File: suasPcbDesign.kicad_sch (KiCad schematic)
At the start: 96 parts, among them J1 SENSE_IB, J2 USB_C_Receptacle_USB2.0_16P, J3 5V Test Pad, J4 3V3 Test Pad, J5 PWM CTRL, J6 JTAG Pinout, J7 SPI OUT, J8 Conn_02x08_Counter_Clockwise, SW1 SW_SPST, SW2 SW_SPST, SW3 SW_SPST, SW4 SW_SPST, SW5 SW_SPST, SW6 SW_SPST, SW7 SW_SPST, U1 LMR51625DDC, U2 MCP3562RT-E/ST, U3 ESP32-S3-WROOM-1, U4 TLV77733PDBVR, U5 USBLC6-2SC6, U7 LM66100DCK, U8 74HC138, U9 LMV331, X7R_Cap1 1uF, X7R_Cap2 1uF, X7R_Cap3 1uF, X7R_Cap4 0.1uF

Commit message: PCB schematic ready to layout
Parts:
- removed J8: Conn_02x08_Counter_Clockwise, Connector_PinHeader_2.54mm:PinHeader_2x08_P2.54mm_Vertical, symbol Connector_Generic:Conn_02x08_Counter_Clockwise
- added J8: Vbat Test Pad, Connector_Wire:SolderWirePad_1x01_SMD_5x10mm, symbol Connector:Conn_01x01_Pin
- added J9: SPI Interface, Connector_PinHeader_2.54mm:PinHeader_2x08_P2.54mm_Vertical, symbol Connector_Generic:Conn_02x08_Odd_Even
- added JP6: VIN Vbat JPR, Jumper:SolderJumper-2_P1.3mm_Open_Pad1.0x1.5mm, symbol Jumper:SolderJumper_2_Open
- Cout_Cap7: value 1uF -> 10uF
- J3, J4: footprint Connector_Wire:SolderWirePad_1x01_SMD_3x6mm -> Connector_Wire:SolderWirePad_1x01_SMD_5x10mm
- U1: footprint DDC0006A-MFG -> Package_TO_SOT_SMD:TSOT-23-6_HandSoldering
- U2: footprint TSSOP20_ST_MCH -> Package_SO:TSSOP-20_4.4x6.5mm_P0.65mm
- U4: footprint TLV -> Package_TO_SOT_SMD:SOT-23-5_HandSoldering
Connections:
- net GND: now also J9.15 (Pin_15)
- net SPI_CC0: now also J9.5 (Pin_5)
- net SPI_CC1: now also J9.7 (Pin_7)
- net SPI_CC2: now also J9.9 (Pin_9)
- net SPI_E0_N: now also J9.11 (Pin_11)
- net SPI_E1_N: now also J9.13 (Pin_13)
- net SPI_E2: now also J9.3 (Pin_3)
- net SPI_PR0: now also J9.2 (Pin_2)
- net SPI_PR1: now also J9.4 (Pin_4)
- net SPI_PR2: now also J9.6 (Pin_6)
- net SPI_PR3: now also J9.8 (Pin_8)
- net SPI_PR4: now also J9.10 (Pin_10)
- net SPI_PR5: now also J9.12 (Pin_12)
- net SPI_PR6: now also J9.14 (Pin_14)
- net SPI_PR7: now also J9.16 (Pin_16)
- net VDD: now also J9.1 (Pin_1)
- net at Cap_13.1, D9.2, U6.3 (+): now also JP6.2 (B); no longer RV1.2
- net at D9.1, JP4.1 (A), U6.1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: now also J8.1 (Pin_1)
- new net: JP6.1 (A), RV1.2
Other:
- moved on the sheet: Cap_13, D9, JP4, U6

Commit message: Fix fotprints
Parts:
- C1: footprint (none) -> Capacitor_SMD:C_0603_1608Metric_Pad1.08x0.95mm_HandSolder
- JP3, JP5: footprint (none) -> TestPoint:TestPoint_2Pads_Pitch2.54mm_Drill0.8mm
- L1: footprint suasPCBFootprints:L_Wurth_WE-MXGI-5030 -> Inductor_SMD:L_APV_APH1050
- R28: footprint (none) -> Resistor_SMD:R_0603_1608Metric_Pad0.98x0.95mm_HandSolder
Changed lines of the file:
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@@
 			)
 		)
-		(property "Footprint" "suasPCBFootprints:L_Wurth_WE-MXGI-5030"
+		(property "Footprint" "Inductor_SMD:L_APV_APH1050"
 			(at 111.76 44.45 0)
 			(hide yes)
@@
 			)
 		)
-		(property "Datasheet" ""
+		(property "Datasheet" "https://www.codaca.com/Private/pdf/CSAB1050A.pdf"
 			(at 111.76 44.45 0)
 			(hide yes)
@@
 			)
 		)
-		(property "Description" "Inductor"
+		(property "Description" "Inductor (CSAB1050A-150M)"
 			(at 111.76 44.45 0)
 			(hide yes)
@@
 			)
 		)
-		(property "Footprint" ""
+		(property "Footprint" "Resistor_SMD:R_0603_1608Metric_Pad0.98x0.95mm_HandSolder"
 			(at 261.112 73.66 90)
 			(hide yes)
@@
 			)
 		)
-		(property "Footprint" ""
+		(property "Footprint" "Capacitor_SMD:C_0603_1608Metric_Pad1.08x0.95mm_HandSolder"
 			(at 388.3152 46.99 0)
 			(hide yes)
@@
 			)
 		)
-		(property "Footprint" ""
+		(property "Footprint" "TestPoint:TestPoint_2Pads_Pitch2.54mm_Drill0.8mm"
 			(at 205.74 160.02 0)
 			(hide yes)
@@
 			)
 		)
-		(property "Footprint" ""
+		(property "Footprint" "TestPoint:TestPoint_2Pads_Pitch2.54mm_Drill0.8mm"
 			(at 219.71 29.21 0)
 			(hide yes)

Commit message: Do the layout
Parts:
- removed D3: ESD9B3.3ST5G, Diode_SMD:D_SOD-923, symbol Diode:ESD9B3.3ST5G
- removed D4: ESD9B5.0ST5G, Diode_SMD:D_SOD-923, symbol Diode:ESD9B5.0ST5G
- removed D7: LED, LED_SMD:LED_0603_1608Metric_Pad1.05x0.95mm_HandSolder, symbol Device:LED
- removed J3: 5V Test Pad, Connector_Wire:SolderWirePad_1x01_SMD_5x10mm, symbol Connector:Conn_01x01_Pin
- removed J4: 3V3 Test Pad, Connector_Wire:SolderWirePad_1x01_SMD_5x10mm, symbol Connector:Conn_01x01_Pin
- removed J8: Vbat Test Pad, Connector_Wire:SolderWirePad_1x01_SMD_5x10mm, symbol Connector:Conn_01x01_Pin
- removed R23: 50R, Resistor_SMD:R_0603_1608Metric_Pad0.98x0.95mm_HandSolder, symbol Device:R
- added D1: SMF5V0A, Diode_SMD:D_SOD-123, symbol Diode:SMF5V0A
- added JP5: GNDA_GND, Jumper:SolderJumper-2_P1.3mm_Open_Pad1.0x1.5mm, symbol Jumper:SolderJumper_2_Open
- H1: footprint MountingHole:MountingHole_6.4mm_M6_Pad_Via -> Custom:7770 Keystone Electronics PC SCREW TERMINALS
- H2: footprint MountingHole:MountingHole_6.4mm_M6 -> Custom:MountingHole_6.3mm_M6_DIN965
- H3: footprint MountingHole:MountingHole_6.4mm_M6_Pad_Via -> Custom:MountingHole_6.3mm_M6_Pad_Via
- J2: renamed from J9; value SPI Interface -> SPI CS
- J4: renamed from J7; value SPI OUT -> SPI CTRL
- J5: footprint Connector_PinSocket_2.54mm:PinSocket_1x03_P2.54mm_Vertical -> Connector_PinHeader_2.54mm:PinHeader_1x03_P2.54mm_Vertical
- renumbered X7R_Cap1 to BBCC1, X7R_Cap2 to BBCC2, X7R_Cap3 to BBCC3, X7R_Cap4 to BBCC4, C4 to C1, C3 to C2, C1 to C3, C2 to C4, Cboot_Cap4 to CBT1, Cin_Cap6 to CIC1, Cout_Cap5 to COC1, Cout_Cap6 to COC2, Cout_Cap7 to COC3, Cap8 to Cap1, Cap9 to Cap2, Cap10 to Cap3, Cap12 to Cap4, Cap11 to Cap5, Cap_15 to Cap_1, Cap_14 to Cap_2, Cap_16 to Cap_3, Cap_17 to Cap_4, Cap_13 to Cap_5, D5 to D2, D9 to D3, D6 to D4, D1 to D5, D8 to D6, D2 to D7, J2 to J7, JP6 to JP1, JP5 to JP2, JP4 to JP3, JP3 to JP3V1, JP1 to JP4, JP2 to JP5V1, R12 to R1, R6 to R10, R7 to R11, R8 to R12, R9 to R13, R10 to R14, R25 to R15, R26 to R16, R16 to R17, R17 to R18, R18 to R19, R13 to R2, R27 to R20, R28 to R21, R19 to R22, R20 to R23, R21 to R24, R24 to R25, R11 to R26, R14 to R3, R15 to R4, R3 to R5, R22 to R6, R1 to R7, R2 to R8, R4 to R9, Rfbt_R3 to RFB1, Rfbb_R4 to RFB2, SW4 to SW1, SW7 to SW2, SW5 to SW3, SW3 to SW4, SW6 to SW5, SW1 to SW6, SW2 to SW7, U8 to U1, U1 to U2, U2 to U3, U6 to U4, U4 to U5, U9 to U6, U3 to U7, U7 to U8, U5 to U9
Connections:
- net 5V: now also D1.1 (A1)
- net GND: now also D1.2 (A2), JP5.2 (B)
- net GNDA: now also JP5.1 (A)
- net SPI_CS: now also JP2.2 (B)

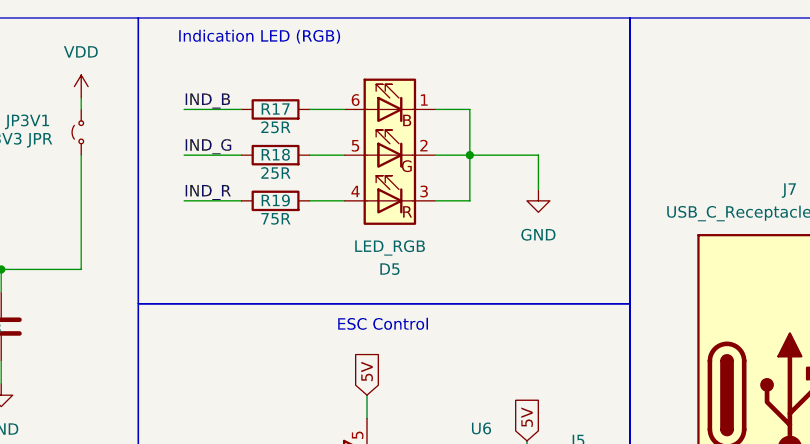
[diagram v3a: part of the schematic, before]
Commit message: Update to use tht led
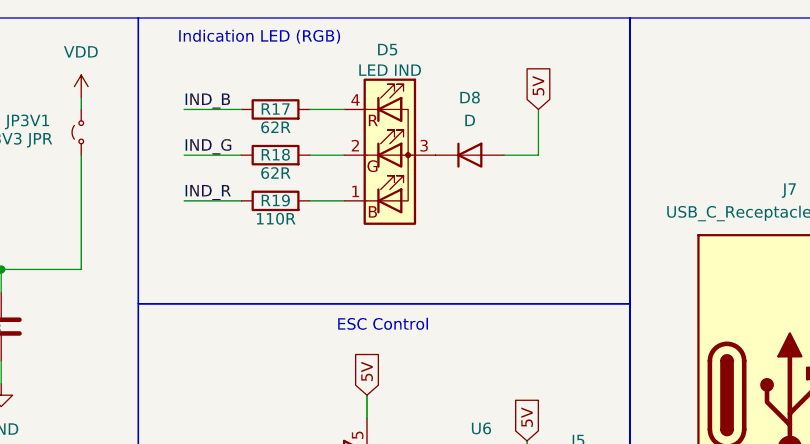
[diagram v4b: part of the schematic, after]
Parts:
- removed D5: LED_RGB, LED_SMD:LED_RGB_PLCC-6, symbol Device:LED_RGB
- added D5: LED IND, LED_THT:LED_D5.0mm-4_RGB, symbol Device:LED_BGAR
- added D8: D, Diode_SMD:D_MiniMELF_Handsoldering, symbol Device:D
- R17, R18: value 25R -> 62R
- R19: value 75R -> 110R
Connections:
- net 5V: now also D8.2 (A)
- net at R19.2: now also D5.1 (BK)
- net at R17.2: now also D5.4 (RK)
- net at R18.2: now also D5.2 (GK)
- new net: D5.3 (A), D8.1 (K)
